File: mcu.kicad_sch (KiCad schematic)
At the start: 29 parts, among them J1 SM03B-SRSS-TB, SW1 SW_Push, SW2 SW_Push, U1 RP2350_60QFN, U2 W25Q128JVS, Y1 ABM8-272-T3

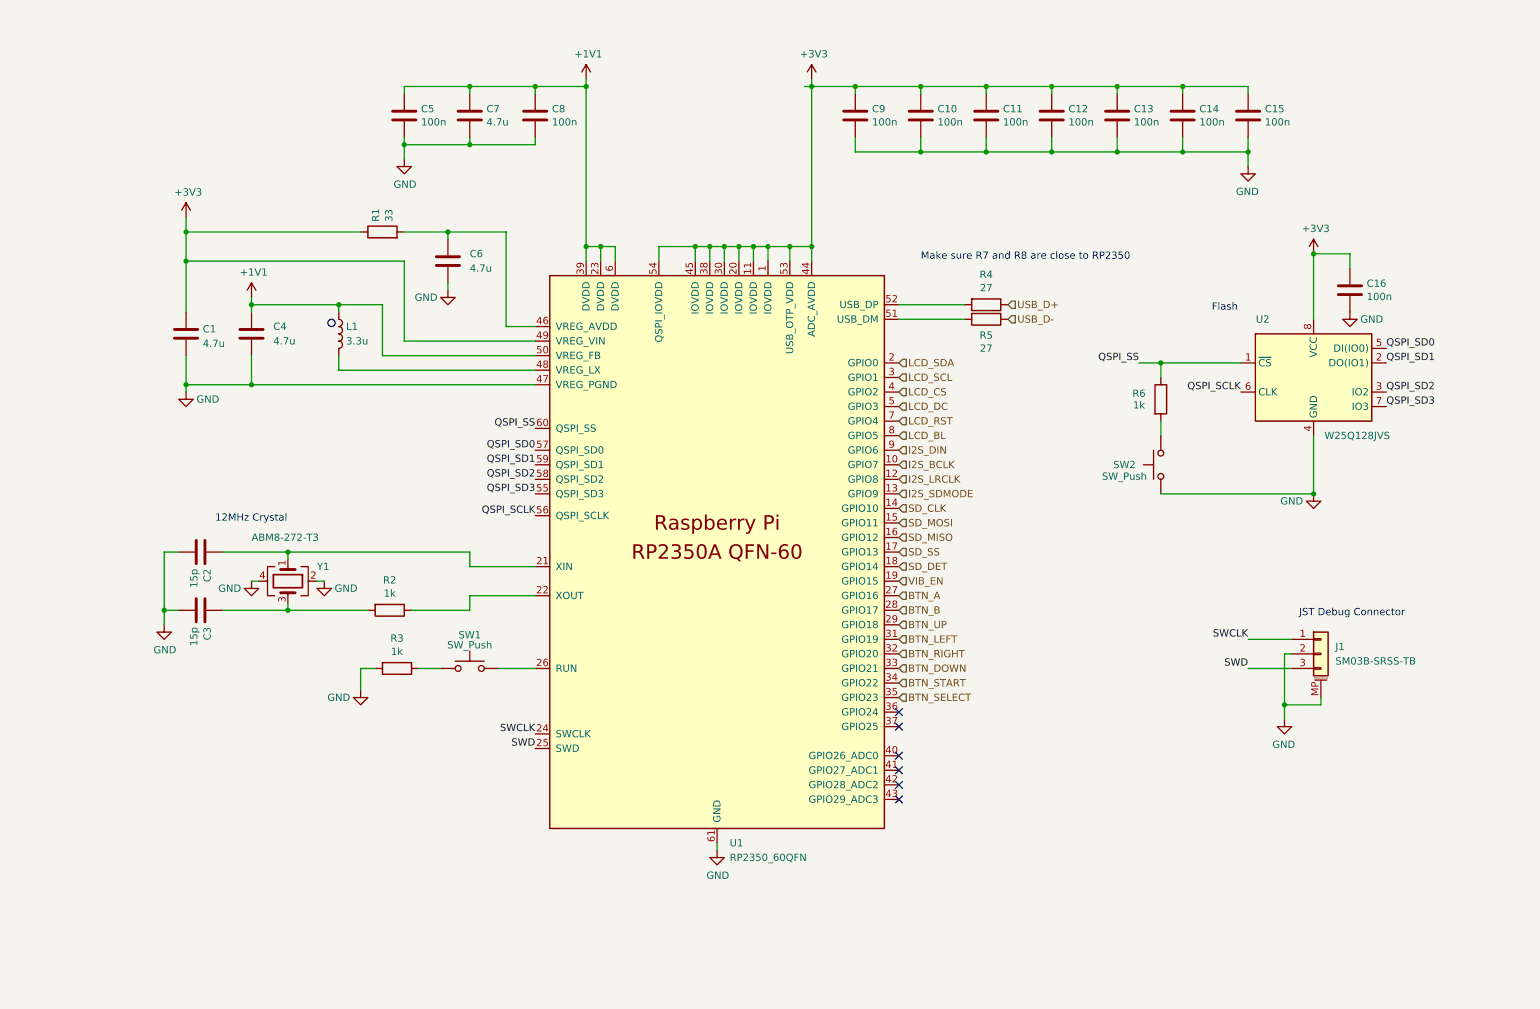
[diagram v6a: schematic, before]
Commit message: check with hardware manual, add comments, add mpns
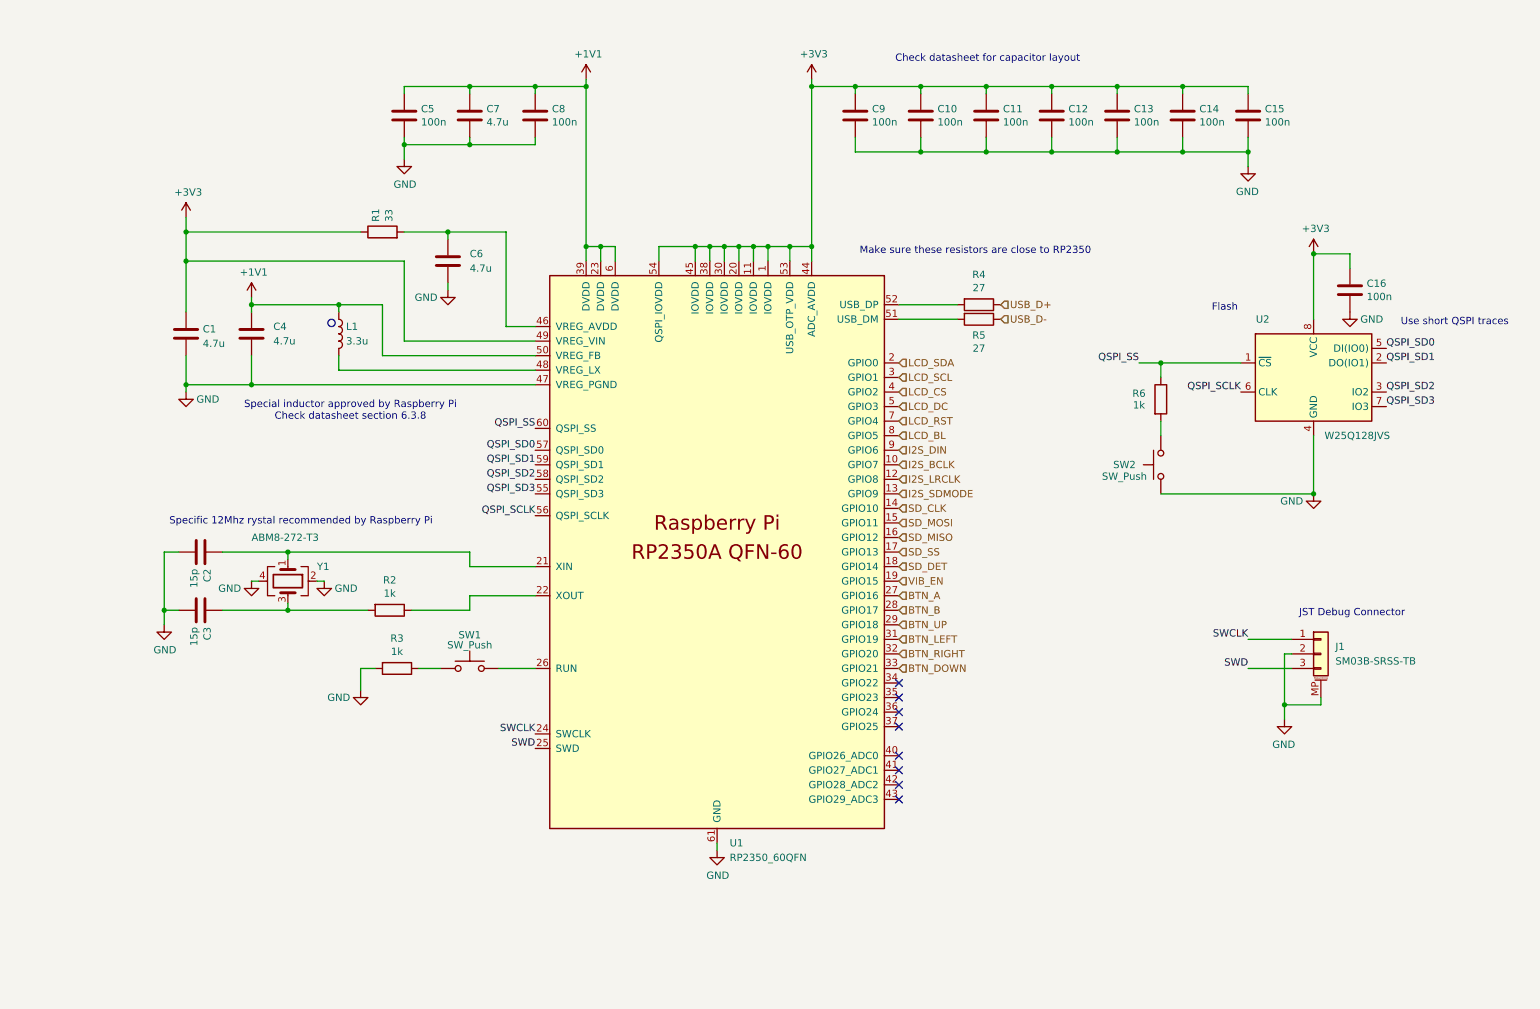
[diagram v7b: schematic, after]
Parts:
- L1: LCSC (none) -> C42411119; Manufacturer (none) -> ABRACON; Manufacturer Part Number (none) -> AOTA-B201610S3R3-101-T
- U1: LCSC (none) -> C42411118; Manufacturer (none) -> Raspberry Pi; Manufacturer Part Number (none) -> RP2350A
- U2: LCSC (none) -> C97521; Manufacturer (none) -> Winbond; Manufacturer Part Number (none) -> W25Q128JVSIQ
- Y1: LCSC (none) -> C20625731; Manufacturer (none) -> ABRACON; Manufacturer Part Number (none) -> ABM8-272-T3
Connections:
- net BTN_SELECT: no longer names the net of U1.35 (GPIO23)
- net BTN_START: no longer names the net of U1.34 (GPIO22)
- no-connect marks 6 -> 8
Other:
- note added: "Check datasheet for capacitor layout"
- note added: "Make sure these resistors are close to RP2350"
- note added: "Special inductor approved by Raspberry Pi Check datasheet section 6.3.8"
- note added: "Specific 12Mhz rystal recommended by Raspberry Pi"
- note added: "Use short QSPI traces"
- note removed: "12MHz Crystal"
- note removed: "Make sure R7 and R8 are close to RP2350"
- moved on the sheet: R4, R5
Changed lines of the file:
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@@
 		)
 	)
-	(text "12MHz Crystal"
+	(text "Check datasheet for capacitor layout"
 		(exclude_from_sim no)
-		(at 55.88 106.68 0)
+		(at 190.754 25.654 0)
+		(effects
+			(font
+				(size 1.27 1.27)
+			)
+		)
+	)
+	(text "Special inductor approved by Raspberry Pi\nCheck datasheet section 6.3.8"
+		(exclude_from_sim no)
+		(at 79.502 87.122 0)
+		(effects
+			(font
+				(size 1.27 1.27)
+			)
+		)
+	)
+	(text "Specific 12Mhz rystal recommended by Raspberry Pi"
+		(exclude_from_sim no)
+		(at 70.866 106.426 0)
+		(effects
+			(font
+				(size 1.27 1.27)
+			)
+		)
+	)
+	(text "Use short QSPI traces"
+		(exclude_from_sim no)
+		(at 272.288 71.628 0)
 		(effects
 			(font
 				(size 1.27 1.27)
 			)
-			(justify left bottom)
 		)
 	)
-	(text "Make sure R7 and R8 are close to RP2350\n"
+	(text "Make sure these resistors are close to RP2350\n"
 		(exclude_from_sim no)
-		(at 179.07 60.96 0)
+		(at 168.402 59.944 0)
 		(effects
 			(font
@@
 	)
 	(no_connect
+		(at 175.26 137.16)
+	)
+	(no_connect
 		(at 175.26 149.86)
 	)
 	(no_connect
+		(at 175.26 134.62)
+	)
+	(no_connect
 		(at 175.26 147.32)
 	)
@@
 	(wire
 		(pts
-			(xy 175.26 71.12) (xy 186.69 71.12)
-		)
-		(stroke
-			(width 0)
-			(type default)
-		)
-	)
-	(wire
-		(pts
 			(xy 50.8 82.55) (xy 62.23 82.55)
 		)
@@
 	(wire
 		(pts
-			(xy 175.26 68.58) (xy 186.69 68.58)
+			(xy 62.23 82.55) (xy 111.76 82.55)
 		)
 		(stroke
@@
 	(wire
 		(pts
-			(xy 62.23 82.55) (xy 111.76 82.55)
+			(xy 224.79 41.91) (xy 213.36 41.91)
 		)
 		(stroke
@@
 	(wire
 		(pts
-			(xy 224.79 41.91) (xy 213.36 41.91)
+			(xy 167.64 39.37) (xy 167.64 41.91)
 		)
 		(stroke
@@
 	(wire
 		(pts
-			(xy 167.64 39.37) (xy 167.64 41.91)
+			(xy 242.57 138.43) (xy 242.57 140.97)
 		)
 		(stroke
@@
 	(wire
 		(pts
-			(xy 242.57 138.43) (xy 242.57 140.97)
+			(xy 254 62.23) (xy 254 59.69)
 		)
 		(stroke
@@
 	(wire
 		(pts
-			(xy 254 62.23) (xy 254 59.69)
+			(xy 149.86 58.42) (xy 152.4 58.42)
 		)
 		(stroke
@@
 	(wire
 		(pts
-			(xy 149.86 58.42) (xy 152.4 58.42)
+			(xy 242.57 138.43) (xy 248.92 138.43)
 		)
 		(stroke
@@
 	(wire
 		(pts
-			(xy 242.57 138.43) (xy 248.92 138.43)
+			(xy 175.26 68.58) (xy 185.42 68.58)
 		)
 		(stroke
@@
 	(wire
 		(pts
-			(xy 158.75 30.48) (xy 160.02 30.48)
-		)
-		(stroke
-			(width 0)
-			(type default)
-		)
-	)
-	(wire
-		(pts
 			(xy 190.5 31.75) (xy 190.5 30.48)
 		)
@@
 	(wire
 		(pts
+			(xy 175.26 71.12) (xy 185.42 71.12)
+		)
+		(stroke
+			(width 0)
+			(type default)
+		)
+	)
+	(wire
+		(pts
 			(xy 120.65 58.42) (xy 120.65 60.96)
 		)
@@
 		)
 	)
-	(hierarchical_label "BTN_START"
-		(shape input)
-		(at 175.26 134.62 0)
-		(effects
-			(font
-				(size 1.27 1.27)
-			)
-			(justify left)
-		)
-	)
 	(hierarchical_label "BTN_B"
 		(shape input)
@@
 	(hierarchical_label "USB_D+"
 		(shape input)
-		(at 194.31 68.58 0)
+		(at 193.04 68.58 0)
 		(effects
 			(font
@@
 	(hierarchical_label "USB_D-"
 		(shape input)
-		(at 194.31 71.12 0)
+		(at 193.04 71.12 0)
 		(effects
 			(font
@@
 		)
 	)
-	(hierarchical_label "BTN_SELECT"
-		(shape input)
-		(at 175.26 137.16 0)
-		(effects
-			(font
-				(size 1.27 1.27)
-			)
-			(justify left)
-		)
-	)
 	(hierarchical_label "LCD_RST"
 		(shape input)
@@
 			)
 		)
-		(property "LCSC" ""
+		(property "LCSC" "C97521"
 			(at 247.65 81.28 0)
 			(effects
@@
 			)
 		)
-		(property "Manufacturer" ""
+		(property "Manufacturer" "Winbond"
 			(at 247.65 81.28 0)
 			(effects
@@
 			)
 		)
-		(property "Manufacturer Part Number" ""
+		(property "Manufacturer Part Number" "W25Q128JVSIQ"
 			(at 247.65 81.28 0)
 			(effects
@@
 			)
 		)
-		(property "Datasheet" ""
+		(property "Datasheet" "https://pip-assets.raspberrypi.com/categories/1214-rp2350/documents/RP-008373-DS-2-rp2350-datasheet.pdf"
 			(at 124.46 111.76 0)
 			(effects
@@
 			)
 		)
-		(property "LCSC" ""
+		(property "LCSC" "C42411118"
 			(at 143.51 111.76 0)
 			(effects
@@
 			)
 		)
-		(property "Manufacturer" ""
+		(property "Manufacturer" "Raspberry Pi"
 			(at 143.51 111.76 0)
 			(effects
@@
 			)
 		)
-		(property "Manufacturer Part Number" ""
+		(property "Manufacturer Part Number" "RP2350A"
 			(at 143.51 111.76 0)
 			(effects
@@
 	(symbol
 		(lib_id "Device:R")
-		(at 190.5 71.12 270)
+		(at 189.23 71.12 270)
 		(unit 1)
 		(exclude_from_sim no)
@@
 		(dnp no)
 		(property "Reference" "R5"
-			(at 190.5 73.914 90)
+			(at 189.23 73.914 90)
 			(effects
 				(font
@@
 		)
 		(property "Value" "27"
-			(at 190.5 76.2 90)
+			(at 189.23 76.2 90)
 			(effects
 				(font
@@
 		)
 		(property "Footprint" "Resistor_SMD:R_0402_1005Metric"
-			(at 190.5 69.342 90)
+			(at 189.23 69.342 90)
 			(effects
 				(font
@@
 		)
 		(property "Datasheet" "~"
-			(at 190.5 71.12 0)
+			(at 189.23 71.12 0)
 			(effects
 				(font
@@
 		)
 		(property "Description" ""
-			(at 190.5 71.12 0)
+			(at 189.23 71.12 0)
 			(effects
 				(font
@@
 			)
 		)
+		(property "LCSC" "C20625731"
+			(at 68.58 116.84 0)
+			(effects
+				(font
+					(size 1.27 1.27)
+				)
+				(hide yes)
+			)
+		)
+		(property "Manufacturer" "ABRACON"
+			(at 68.58 116.84 0)
+			(effects
+				(font
+					(size 1.27 1.27)
+				)
+				(hide yes)
+			)
+		)
+		(property "Manufacturer Part Number" "ABM8-272-T3"
+			(at 68.58 116.84 0)
+			(effects
+				(font
+					(size 1.27 1.27)
+				)
+				(hide yes)
+			)
+		)
 		(pin "1"
 		)
@@
 			)
 		)
+		(property "LCSC" "C42411119"
+			(at 77.47 73.66 0)
+			(effects
+				(font
+					(size 1.27 1.27)
+				)
+				(hide yes)
+			)
+		)
+		(property "Manufacturer" "ABRACON"
+			(at 77.47 73.66 0)
+			(effects
+				(font
+					(size 1.27 1.27)
+				)
+				(hide yes)
+			)
+		)
+		(property "Manufacturer Part Number" "AOTA-B201610S3R3-101-T"
+			(at 77.47 73.66 0)
+			(effects
+				(font
+					(size 1.27 1.27)
+				)
+				(hide yes)
+			)
+		)
 		(pin "1"
 		)
@@
 	(symbol
 		(lib_id "Device:R")
-		(at 190.5 68.58 270)
+		(at 189.23 68.58 270)
 		(unit 1)
 		(exclude_from_sim no)
@@
 		(dnp no)
 		(property "Reference" "R4"
-			(at 190.5 63.3222 90)
+			(at 189.23 63.3222 90)
 			(effects
 				(font
@@
 		)
 		(property "Value" "27"
-			(at 190.5 65.6336 90)
+			(at 189.23 65.6336 90)
 			(effects
 				(font
@@
 		)
 		(property "Footprint" "Resistor_SMD:R_0402_1005Metric"
-			(at 190.5 66.802 90)
+			(at 189.23 66.802 90)
 			(effects
 				(font
@@
 		)
 		(property "Datasheet" "~"
-			(at 190.5 68.58 0)
+			(at 189.23 68.58 0)
 			(effects
 				(font
@@
 		)
 		(property "Description" ""
-			(at 190.5 68.58 0)
+			(at 189.23 68.58 0)
 			(effects
 				(font

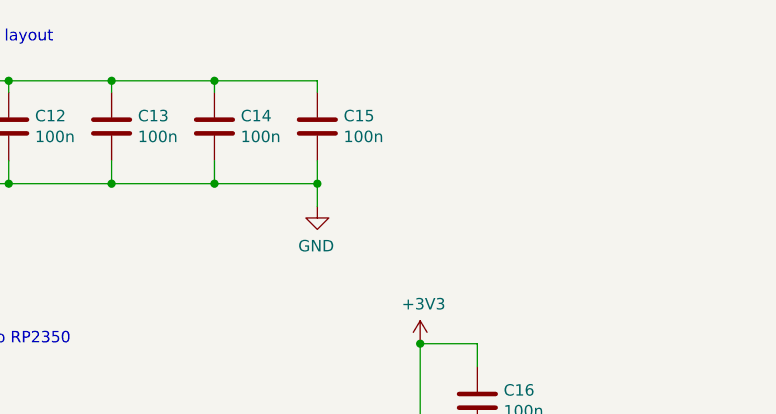
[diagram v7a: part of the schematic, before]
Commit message: place mcu on board
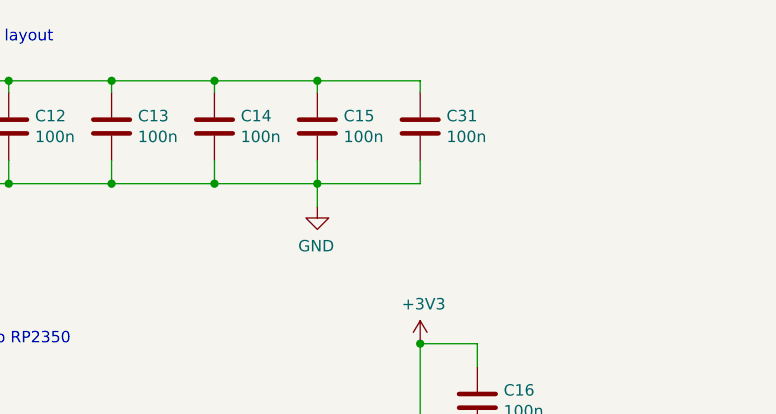
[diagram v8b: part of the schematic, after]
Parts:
- added C31: 100n, Capacitor_SMD:C_0402_1005Metric, symbol Device:C
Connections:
- net +3V3: now also C31.1
- net GND: now also C31.2
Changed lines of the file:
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@@
+	)
+	(junction
+		(at 236.22 30.48)
+		(diameter 0)
+		(color 0 0 0 0)
 	)
 	(junction
@@
 	(wire
 		(pts
+			(xy 247.65 31.75) (xy 247.65 30.48)
+		)
+		(stroke
+			(width 0)
+			(type default)
+		)
+	)
+	(wire
+		(pts
 			(xy 68.58 120.65) (xy 68.58 121.92)
 		)
@@
 	(wire
 		(pts
+			(xy 247.65 39.37) (xy 247.65 41.91)
+		)
+		(stroke
+			(width 0)
+			(type default)
+		)
+	)
+	(wire
+		(pts
 			(xy 247.65 59.69) (xy 247.65 71.12)
 		)
@@
 	(wire
 		(pts
+			(xy 236.22 30.48) (xy 247.65 30.48)
+		)
+		(stroke
+			(width 0)
+			(type default)
+		)
+	)
+	(wire
+		(pts
 			(xy 88.9 31.75) (xy 88.9 30.48)
 		)
@@
 		(pts
 			(xy 125.73 58.42) (xy 125.73 60.96)
+		)
+		(stroke
+			(width 0)
+			(type default)
+		)
+	)
+	(wire
+		(pts
+			(xy 236.22 41.91) (xy 247.65 41.91)
 		)
 		(stroke
@@
 					(unit 1)
 				)
+			)
+		)
+	)
+	(symbol
+		(lib_id "Device:C")
+		(at 247.65 35.56 0)
+		(unit 1)
+		(exclude_from_sim no)
+		(in_bom yes)
+		(on_board yes)
+		(dnp no)
+		(property "Reference" "C31"
+			(at 250.571 34.3916 0)
+			(effects
+				(font
+					(size 1.27 1.27)
+				)
+				(justify left)
+			)
+		)
+		(property "Value" "100n"
+			(at 250.571 36.703 0)
+			(effects
+				(font
+					(size 1.27 1.27)
+				)
+				(justify left)
+			)
+		)
+		(property "Footprint" "Capacitor_SMD:C_0402_1005Metric"
+			(at 248.6152 39.37 0)
+			(effects
+				(font
+					(size 1.27 1.27)
+				)
+				(hide yes)
+			)
+		)
+		(property "Datasheet" "~"
+			(at 247.65 35.56 0)
+			(effects
+				(font
+					(size 1.27 1.27)
+				)
+				(hide yes)
+			)
+		)
+		(property "Description" ""
+			(at 247.65 35.56 0)
+			(effects
+				(font
+					(size 1.27 1.27)
+				)
+			)
+		)
+		(pin "1"
+		)
+		(pin "2"
+		)
+		(instances
+			(project "gameboy"
+				(path "/f4643692-c319-40a7-82a2-3e775c0a417f/0c43a605-cda2-4793-9a29-301f6419db25"
+					(reference "C31")
+					(unit 1)
+				)
